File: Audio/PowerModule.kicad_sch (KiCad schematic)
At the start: 15 parts, among them J4 PWR_IN, J5 PWR_OUT, U1 MCW03

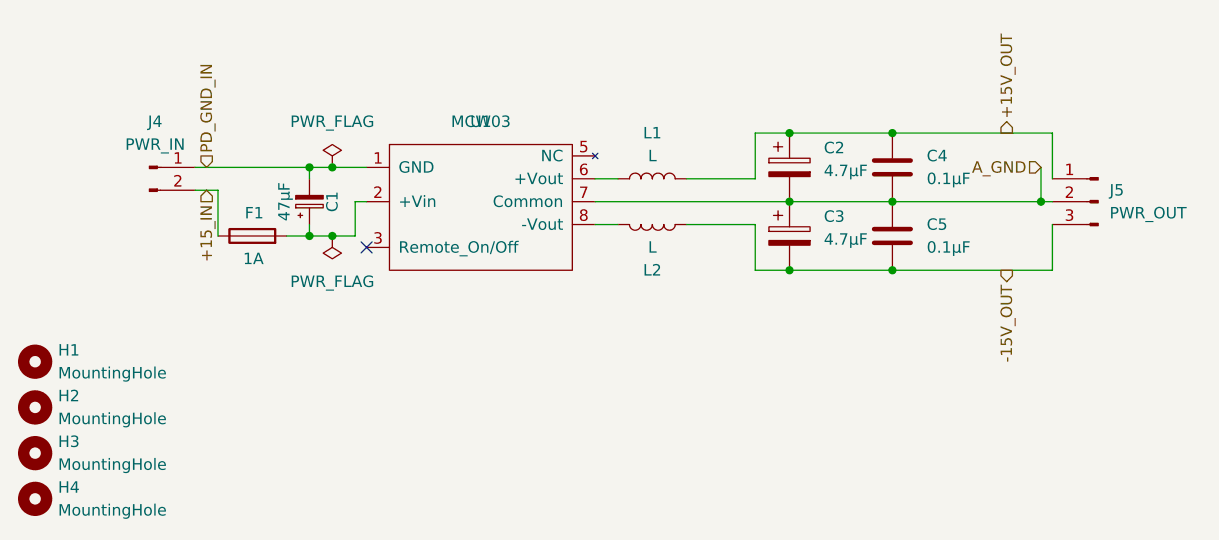
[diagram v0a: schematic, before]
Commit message: PowerModuleをTEC 3-1223前提でリファインし、Cout/LC計算を文書化する。
AmpのSMD 100µF電源バッファを仕様内に載せるためMCW03(47µF上限)から
TEC 3-1223(440µF上限)へ置き換え、二次LC(10µH+22µF)と入力EMI方針を固定する。

Co-authored-by: m_arino <indare@users.noreply.github.com>
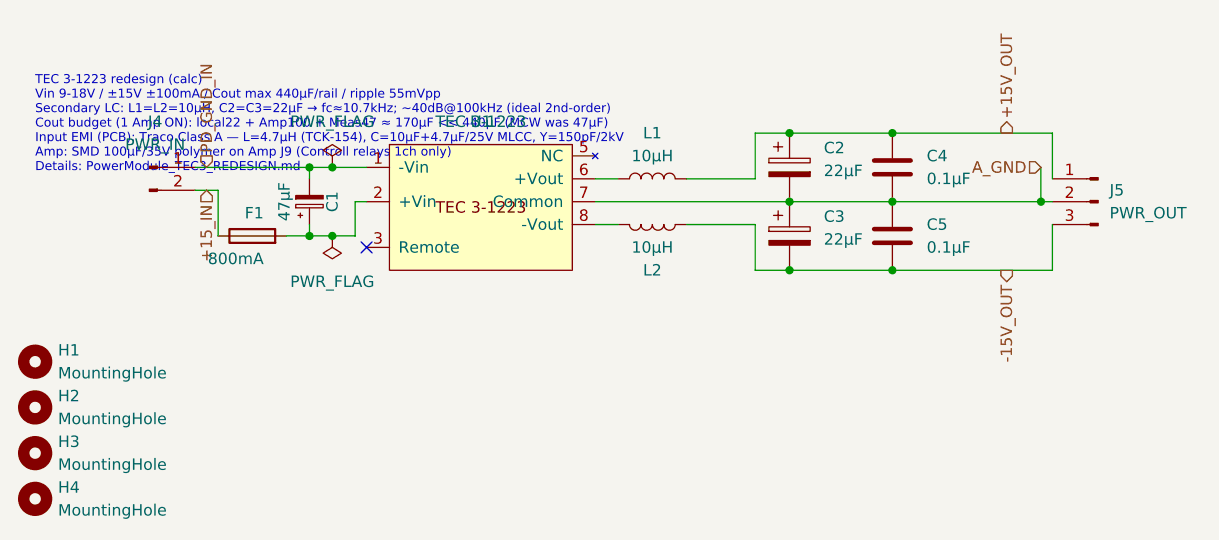
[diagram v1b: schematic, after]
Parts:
- C1: value 47μF -> 47µF
- C2, C3: value 4.7μF -> 22µF; footprint Capacitor_THT:CP_Radial_D5.0mm_P2.00mm -> Capacitor_SMD:CP_Elec_5x5.3
- C4, C5: value 0.1μF -> 0.1µF
- F1: value 1A -> 800mA
- L1, L2: value L -> 10µH; footprint Inductor_SMD:L_12x12mm_H8mm -> Inductor_SMD:L_1210_3225Metric
- U1: value MCW03 -> TEC 3-1223; footprint Library:MCW03-12D15_SIP7_THT -> Library:TEC3-1223_SIP8_THT; symbol MCW03:MCW03-12D15 -> TEC3:TEC3-1223
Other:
- note added: "TEC 3-1223 redesign (calc) Vin 9-18V / ±15V ±100mA / Cout max 440µF/rail / ripple 55mVpp Secondary LC: L1=L2=10µH, C2=C3=22µF → fc≈10.7kHz; ~40dB@100kHz (ideal 2nd-order) Cout budget (1 Amp ON): local22 + Amp100 + Meas47 ≈ 170µF << 440µF (MCW was 47µF) Input EMI (PCB): Traco Class A — L=4.7µH (TCK-154), C=10µF+4.7µF/25V MLCC, Y=150pF/2kV Amp: SMD 100µF/35V polymer on Amp J9 (Controll relays 1ch o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"
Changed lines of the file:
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@@
 		)
+	)
+	(text "TEC 3-1223 redesign (calc)\nVin 9-18V / ±15V ±100mA / Cout max 440µF/rail / ripple 55mVpp\nSecondary LC: L1=L2=10µH, C2=C3=22µF → fc≈10.7kHz; ~40dB@100kHz (ideal 2nd-order)\nCout budget (1 Amp ON): local22 + Amp100 + Meas47 ≈ 170µF << 440µF (MCW was 47µF)\nInput EMI (PCB): Traco Class A — L=4.7µH (TCK-154), C=10µF+4.7µF/25V MLCC, Y=150pF/2kV\nAmp: SMD 100µF/35V polymer on Amp J9 (Controll relays 1ch only)\nDetails: PowerModule_TEC3_REDESIGN.md"
+		(exclude_from_sim no)
+		(at 15.24 26.67 0)
+		(effects
+			(font
+				(size 1.0 1.0)
+			)
+			(justify left top)
+		)
+		(uuid "b0a0tec3-0001-4000-8000-000000000001")
 	)
 	(hierarchical_label "A_GND"
@@
 			)
 		)
-		(property "Value" "L"
+		(property "Value" "10µH"
 			(at 83.82 35.56 90)
 			(show_name no)
@@
 			)
 		)
-		(property "Footprint" "Inductor_SMD:L_12x12mm_H8mm"
+		(property "Footprint" "Inductor_SMD:L_1210_3225Metric"
 			(at 83.82 38.1 0)
 			(hide yes)
@@
 			)
 		)
-		(property "Description" "Inductor"
+		(property "Description" "Secondary LC +15: 10uH, Isat>=0.3A. fc~10.7kHz with C2=22uF"
 			(at 83.82 38.1 0)
 			(hide yes)
@@
 			)
 		)
-		(property "Value" "47μF"
+		(property "Value" "47µF"
 			(at 42.926 40.64 90)
 			(show_name no)
@@
 			)
 		)
-		(property "Description" "Polarized capacitor, small symbol"
+		(property "Description" "12V input bulk after fuse. PCB: add Traco Class-A L=4.7uH + 10uF/4.7uF MLCC at U1 Vin"
 			(at 45.72 40.64 0)
 			(hide yes)
@@
 			)
 		)
-		(property "Value" "0.1μF"
+		(property "Value" "0.1µF"
 			(at 114.3 45.7199 0)
 			(show_name no)
@@
 			)
 		)
-		(property "Description" "Unpolarized capacitor"
+		(property "Description" "-15 HF ceramic at bus"
 			(at 110.49 44.45 0)
 			(hide yes)
@@
 	)
 	(symbol
-		(lib_id "MCW03:MCW03-12D15")
+		(lib_id "TEC3:TEC3-1223")
 		(at 64.77 31.75 0)
 		(unit 1)
@@
 			)
 		)
-		(property "Value" "MCW03"
+		(property "Value" "TEC 3-1223"
 			(at 64.77 31.75 0)
 			(show_name no)
@@
 			)
 		)
-		(property "Footprint" "Library:MCW03-12D15_SIP7_THT"
+		(property "Footprint" "Library:TEC3-1223_SIP8_THT"
 			(at 66.04 27.94 0)
 			(hide yes)
@@
 			)
 		)
-		(property "Datasheet" "file://C:\\Users\\masas\\Desktop\\PCB\\equalizer\\MCW03.pdf"
+		(property "Datasheet" "https://www.tracopower.com/sites/default/files/products/datasheets/tec3_datasheet.pdf"
 			(at 65.278 29.972 0)
 			(hide yes)
@@
 			)
 		)
-		(property "Value" "4.7μF"
+		(property "Value" "22µF"
 			(at 102.87 37.2109 0)
 			(show_name no)
@@
 			)
 		)
-		(property "Footprint" "Capacitor_THT:CP_Radial_D5.0mm_P2.00mm"
+		(property "Footprint" "Capacitor_SMD:CP_Elec_5x5.3"
 			(at 100.0252 40.64 0)
 			(hide yes)
@@
 			)
 		)
-		(property "Description" "Polarized capacitor"
+		(property "Description" "+15 after L1: polymer/OS-CON 22uF 35V. Part of Cout budget"
 			(at 99.06 36.83 0)
 			(hide yes)
@@
 			)
 		)
-		(property "Value" "L"
+		(property "Value" "10µH"
 			(at 83.82 45.72 90)
 			(show_name no)
@@
 			)
 		)
-		(property "Footprint" "Inductor_SMD:L_12x12mm_H8mm"
+		(property "Footprint" "Inductor_SMD:L_1210_3225Metric"
 			(at 83.82 43.18 0)
 			(hide yes)
@@
 			)
 		)
-		(property "Description" "Inductor"
+		(property "Description" "Secondary LC -15: 10uH, Isat>=0.3A. fc~10.7kHz with C3=22uF"
 			(at 83.82 43.18 0)
 			(hide yes)
@@
 			)
 		)
-		(property "Value" "4.7μF"
+		(property "Value" "22µF"
 			(at 102.87 44.8309 0)
 			(show_name no)
@@
 			)
 		)
-		(property "Footprint" "Capacitor_THT:CP_Radial_D5.0mm_P2.00mm"
+		(property "Footprint" "Capacitor_SMD:CP_Elec_5x5.3"
 			(at 100.0252 48.26 0)
 			(hide yes)
@@
 			)
 		)
-		(property "Description" "Polarized capacitor"
+		(property "Description" "-15 after L2: polymer/OS-CON 22uF 35V. Part of Cout budget"
 			(at 99.06 44.45 0)
 			(hide yes)
@@
 			)
 		)
-		(property "Value" "0.1μF"
+		(property "Value" "0.1µF"
 			(at 114.3 38.0999 0)
 			(show_name no)
@@
 			)
 		)
-		(property "Description" "Unpolarized capacitor"
+		(property "Description" "+15 HF ceramic at bus"
 			(at 110.49 36.83 0)
 			(hide yes)
@@
 			)
 		)
-		(property "Value" "1A"
+		(property "Value" "800mA"
 			(at 40.64 46.99 90)
 			(show_name no)
@@
 			)
 		)
-		(property "Description" "Fuse"
+		(property "Description" "Traco TEC3-12xx recommended input fuse 0.8A slow-blow"
 			(at 39.37 44.45 0)
 			(hide yes)
